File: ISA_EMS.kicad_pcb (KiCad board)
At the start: 2 copper layers, 176.5 x 102.9 mm, 57 parts, among them J1 ISA BUS, J2 EMS Address, J3 ROM Config, U1 74HCT688, U10 74HCT32, U11 74HCT04, U12 74ACT245, U13 AS6C4008-55PCN, U14 AS6C4008-55PCN, U15 AS6C4008-55PCN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

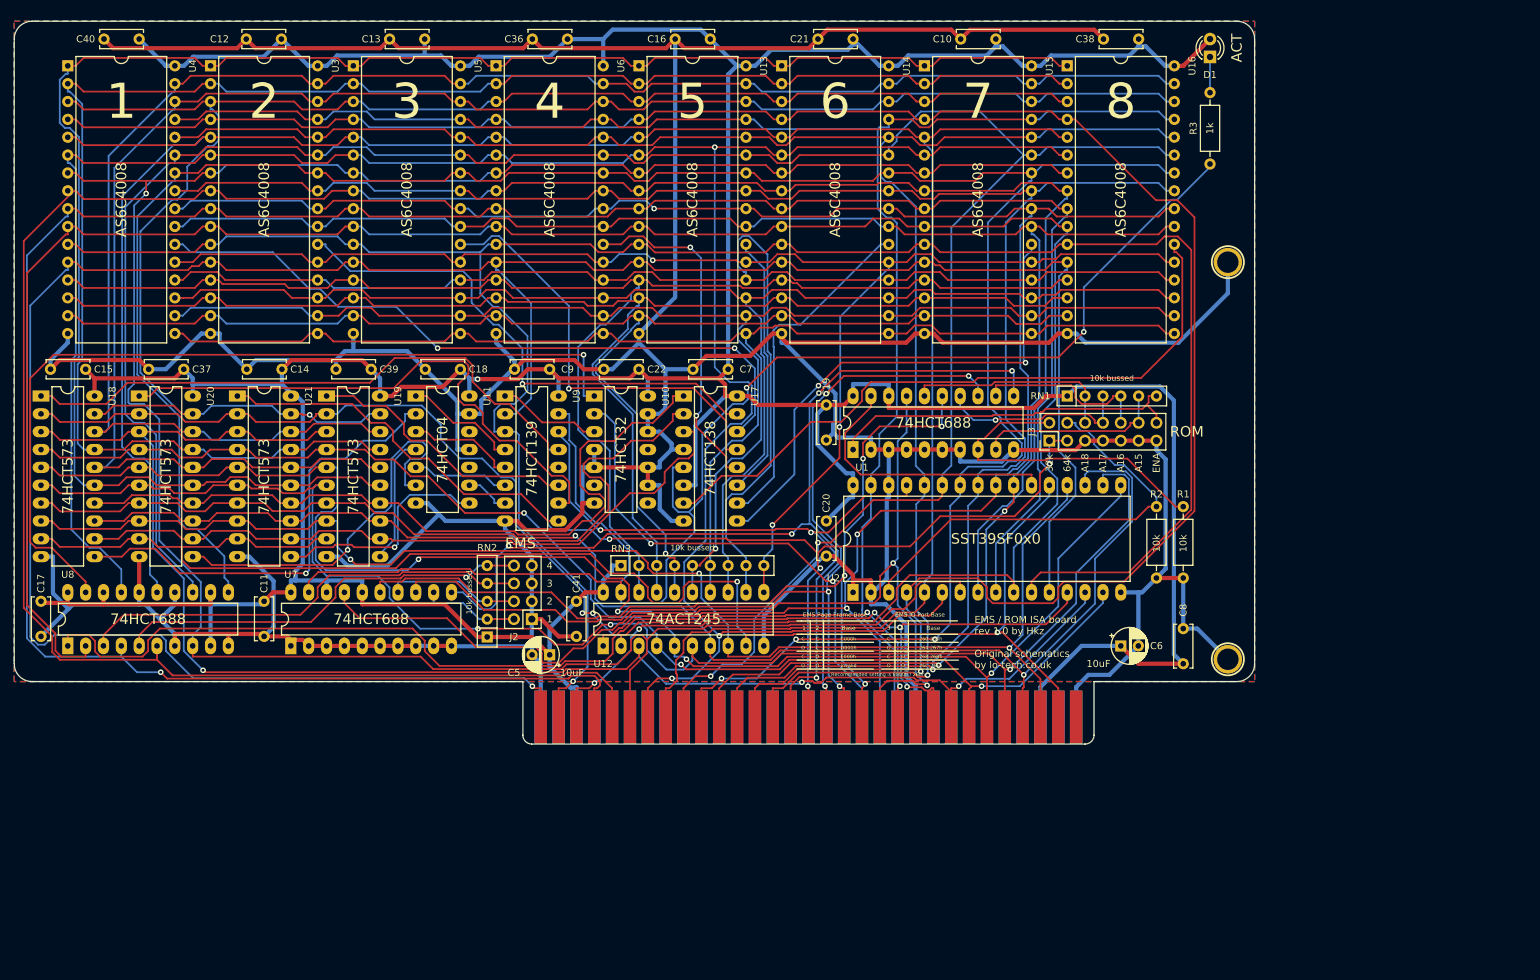
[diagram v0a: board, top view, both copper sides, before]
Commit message: Begin removing useless components
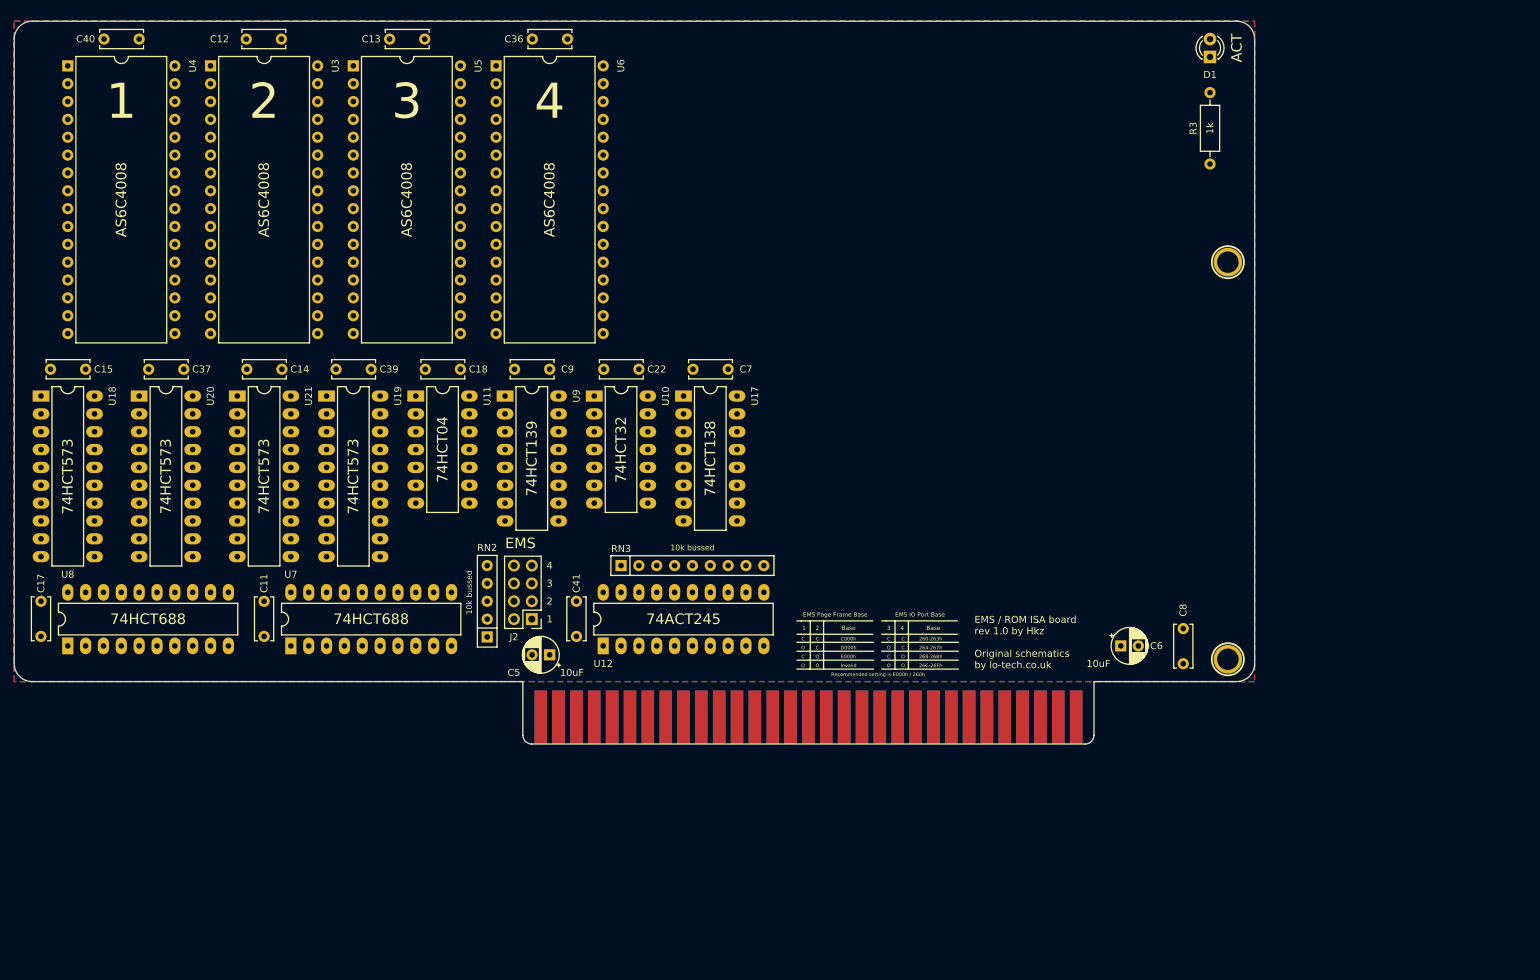
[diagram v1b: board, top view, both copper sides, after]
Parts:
- removed C10, C16, C19, C20, C21, C38: 100nF, Capacitor_THT:C_Disc_D6.0mm_W2.5mm_P5.00mm
- removed J3: ROM Config, Connector_PinHeader_2.54mm:PinHeader_2x07_P2.54mm_Vertical
- removed R1, R2: 10k, Resistor_THT:R_Axial_DIN0207_L6.3mm_D2.5mm_P10.16mm_Horizontal
- removed RN1: 10k, Resistor_THT:R_Array_SIP6
- removed U1: 74HCT688, Package_DIP:DIP-20_W7.62mm_LongPads
- removed U13, U14, U15, U16: AS6C4008-55PCN, Package_DIP:DIP-32_W15.24mm
- removed U2: SST39SF040, Package_DIP:DIP-32_W15.24mm_LongPads
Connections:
- U17 pad 10: /~RAM-CS5 -> (no net)
- U17 pad 11: /~RAM-CS4 -> (no net)
- U17 pad 7: /~RAM-CS7 -> (no net)
- U17 pad 9: /~RAM-CS6 -> (no net)
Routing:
- net GND: track 884.8 -> 0.00 mm
- net VCC: track 681.1 -> 0.00 mm, vias 1 -> 0
- net /A4: track 370.6 -> 0.00 mm
- net /A3: track 363.3 -> 0.00 mm, vias 1 -> 0
- net /A0: track 362.7 -> 0.00 mm, vias 1 -> 0
- net /A5: track 354.4 -> 0.00 mm, vias 1 -> 0
- net /A2: track 353.8 -> 0.00 mm, vias 2 -> 0
- net /A6: track 349.8 -> 0.00 mm, vias 3 -> 0
- net /A7: track 340.5 -> 0.00 mm
- net /A9: track 337.3 -> 0.00 mm, vias 3 -> 0
- net /A8: track 334.0 -> 0.00 mm, vias 2 -> 0
- net /A1: track 315.3 -> 0.00 mm, vias 1 -> 0
- net /A12: track 306.1 -> 0.00 mm, vias 1 -> 0
- net /~MEMR: track 282.7 -> 0.00 mm, vias 3 -> 0
- net /A11: track 261.1 -> 0.00 mm, vias 1 -> 0
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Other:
- board text removed: "10k"
- board text removed: "32k"
- board text removed: "5"
- board text removed: "6"
- board text removed: "64k"
- board text removed: "7"
- board text removed: "8"
- board text removed: "A15"
- board text removed: "A16"
- board text removed: "A17"
- board text removed: "A18"
- board text removed: "ENA"
- board text removed: "ROM"
- board text removed: "SST39SF0x0"

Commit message: Begin moving components
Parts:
- moved U5 81.3 mm to (268.0, 106.7)
- moved U6 81.3 mm to (288.3, 106.7)
- moved C12 81.3 mm to (252.7, 102.9)
- moved C13 81.3 mm to (278.1, 102.9)
- moved C36 81.3 mm to (298.4, 102.9)
- moved C40 81.3 mm to (237.5, 102.9)
- moved U3 81.3 mm to (247.7, 106.7)
- moved U4 81.3 mm to (227.3, 106.7)
- moved C39 69.6 mm to (258.8, 149.6)
- moved U10 69.6 mm to (290.6, 153.4)
- moved C14 69.6 mm to (246.1, 149.6)
- moved C15 69.6 mm to (218.2, 149.6)
- moved C18 69.6 mm to (271.5, 149.6)
- moved C37 69.6 mm to (232.2, 149.6)
- moved C9 69.6 mm to (284.2, 149.6)
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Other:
- board text added: "EMS 2MB ISA board rev 1.0 by Hkz Original schematics by lo-tech.co.uk"
- board text removed: "EMS / ROM ISA board rev 1.0 by Hkz Original schematics by lo-tech.co.uk"

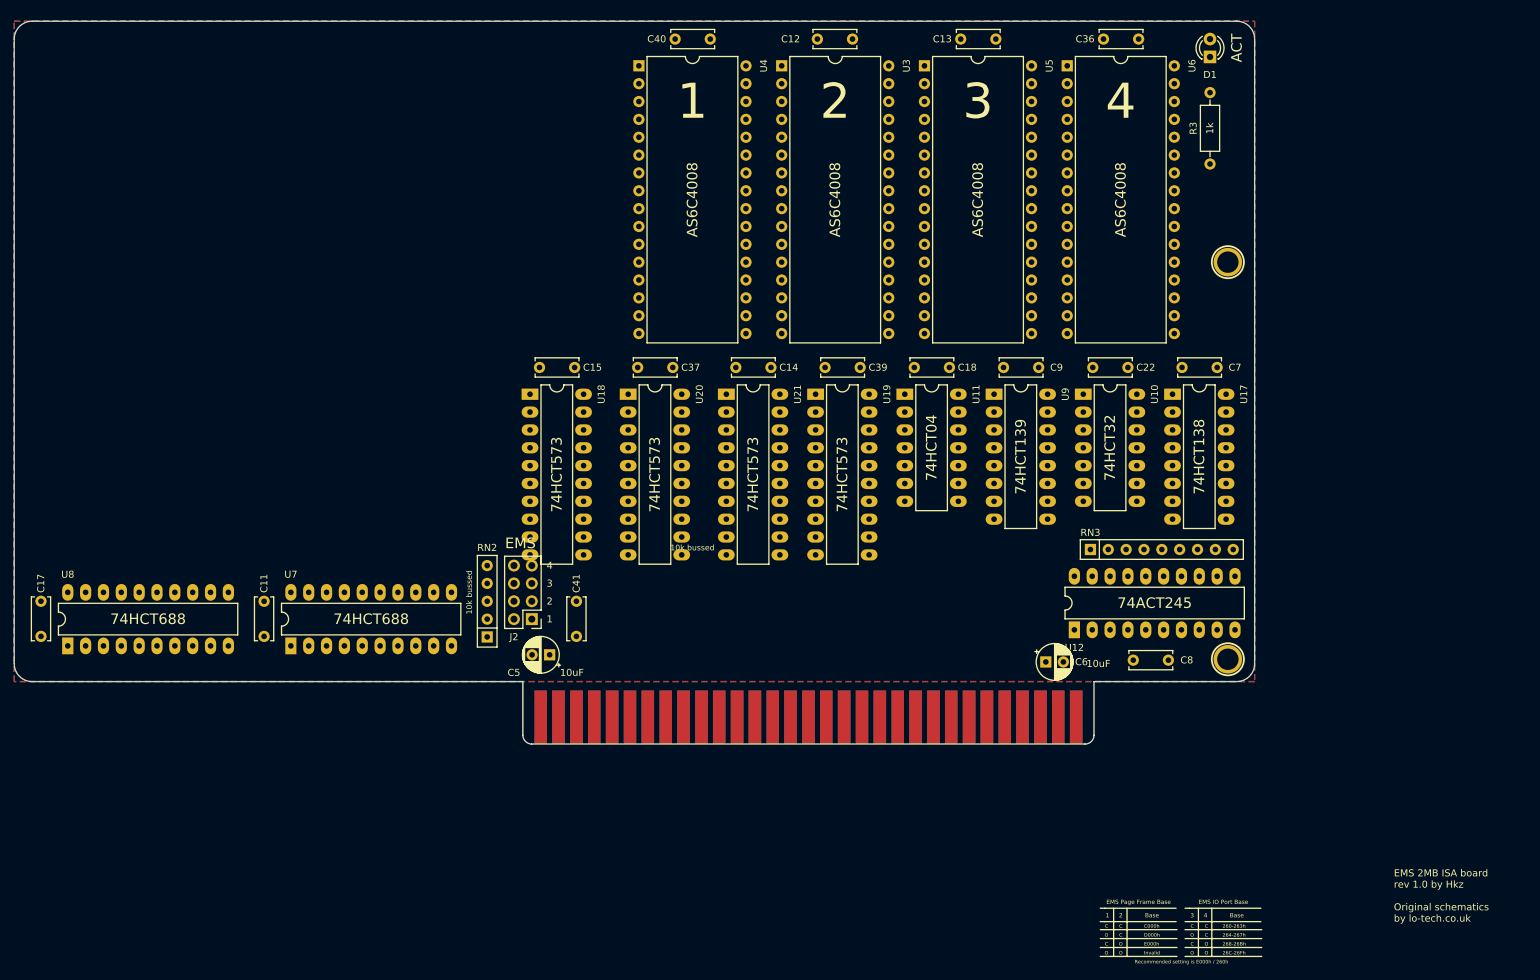
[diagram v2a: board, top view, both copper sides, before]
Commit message: moved components on card
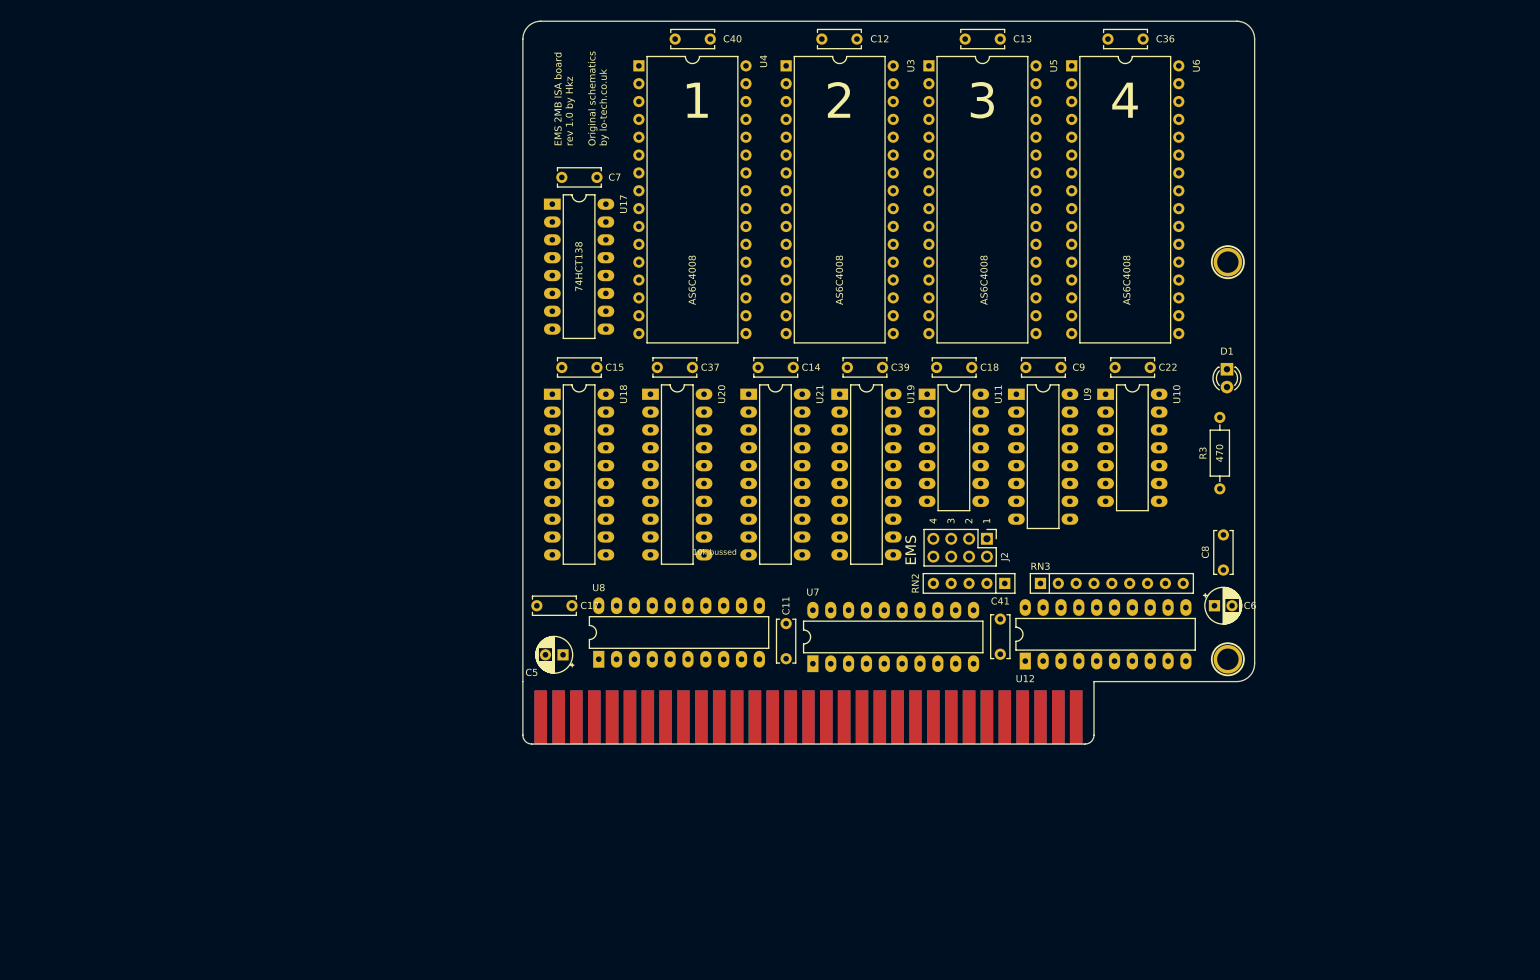
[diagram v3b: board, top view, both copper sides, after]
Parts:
- R3: value 1k -> 470
- U3, U4, U5, U6: value AS6C4008-55PCN -> AS6C4008
- moved U17 92.3 mm to (215.0, 126.4)
- moved C7 92.3 mm to (221.4, 122.6)
- moved U8 75.6 mm to (221.6, 191.1)
- moved C17 75.6 mm to (217.8, 183.5), turned to 180 degrees
- moved C11 74.4 mm to (248.3, 186.1)
- moved U7 74.3 mm to (252.1, 191.8)
- moved RN2 74.1 mm to (279.4, 180.3), turned to 180 degrees
- moved J2 65.8 mm to (276.9, 174.0), turned to 270 degrees
- moved C41 60.4 mm to (278.8, 185.4)
- moved R3 46.2 mm to (310.0, 166.9)
- moved D1 44.5 mm to (311.0, 149.9), turned to 270 degrees
- moved C6 25.3 mm to (309.2, 183.5)
- moved C8 18.1 mm to (310.5, 178.4), turned to 90 degrees
- moved RN3 8.59 mm to (284.5, 180.3)
- moved U12 8.28 mm to (282.3, 191.4)
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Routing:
- removed copper zone on B.Cu, net GND
- removed copper zone on F.Cu, net GND
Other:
- board size 176.5 x 102.9 mm -> 104.1 x 102.9 mm
- board text removed: "10uF"
- board text removed: "1k"
- board text removed: "74ACT245"
- board text removed: "74HCT04"
- board text removed: "74HCT138"
- board text removed: "74HCT139"
- board text removed: "74HCT32"
- board text removed: "74HCT573"
- board text removed: "74HCT688"
- board text removed: "ACT"
- board text removed: "AS6C4008"

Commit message: Add silkscreen
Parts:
- U18, U19, U20, U21: value 74LS573 -> 74HCT573
- U3, U4, U5, U6: value AS6C4008 -> AS6C4008-55PCN
- moved RN3 0.90 mm to (285.1, 179.7)
- moved C11 0.64 mm to (248.3, 185.4)
- moved U7 0.64 mm to (252.1, 191.1)
- moved C6 0.63 mm to (309.9, 183.5)
- moved U12 0.25 mm to (282.3, 191.1)
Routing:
- net GND: track 0.00 -> 567.4 mm
- net VCC: track 0.00 -> 478.1 mm, vias 0 -> 1
- net /~RAM-SELECT: track 0.00 -> 271.8 mm, vias 0 -> 1
- net /A0: track 0.00 -> 179.6 mm
- net /RAM-A14: track 0.00 -> 174.0 mm, vias 0 -> 1
- net /A1: track 0.00 -> 172.4 mm, vias 0 -> 1
- net /A5: track 0.00 -> 172.3 mm
- net /RAM-A18: track 0.00 -> 170.6 mm
- net /RAM-A16: track 0.00 -> 163.7 mm
- net /A4: track 0.00 -> 163.6 mm, vias 0 -> 1
- net /~MEMW: track 0.00 -> 161.9 mm
- net /RAM-A15: track 0.00 -> 161.7 mm
- net /RAM-A17: track 0.00 -> 160.6 mm
- net /~MEMR: track 0.00 -> 159.6 mm, vias 0 -> 1
- net /A7: track 0.00 -> 157.1 mm, vias 0 -> 1
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- added copper zone on B.Cu, net GND
- added copper zone on F.Cu, net GND
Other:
- board text removed: "10k bussed"

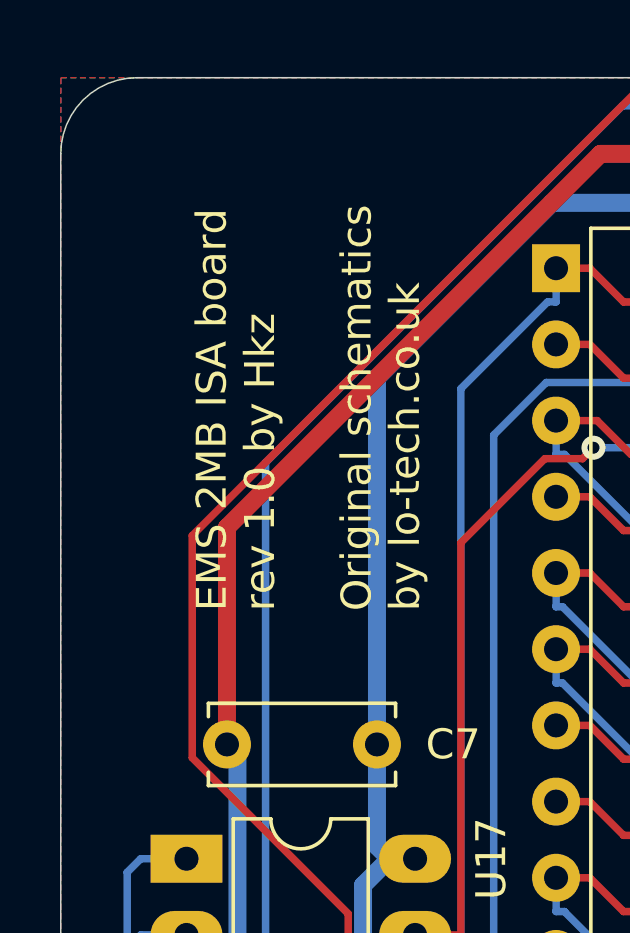
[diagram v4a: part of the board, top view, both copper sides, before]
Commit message: add via to board and refill
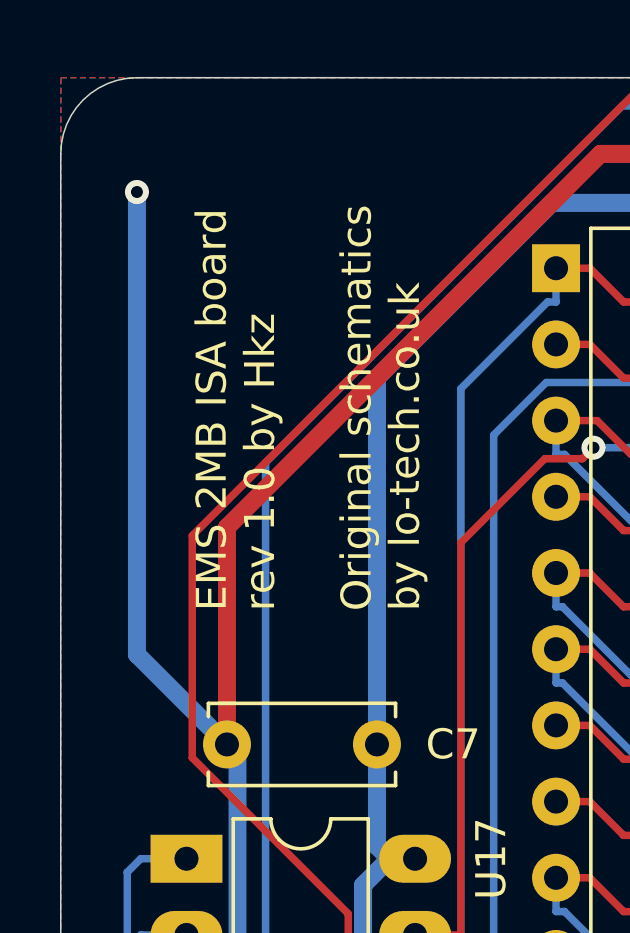
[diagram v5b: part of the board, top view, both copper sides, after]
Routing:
- net GND: track 567.4 -> 587.1 mm, vias 0 -> 1
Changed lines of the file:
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@@
     (thickness 1.6)
     (drawings 83)
-    (tracks 2016)
+    (tracks 2019)
     (zones 0)
     (modules 41)
@@
   (page A3)
   (layers
-    (0 F.Cu signal hide)
-    (31 B.Cu signal hide)
+    (0 F.Cu signal)
+    (31 B.Cu signal)
     (32 B.Adhes user)
     (33 F.Adhes user)
@@
     (arrow2b (pts (xy 314.96 199.39) (xy 313.833496 199.976421)))
   )
+  (via (at 213.36 104.14) (size 0.8) (drill 0.4) (layers F.Cu B.Cu) (net 1))
   (segment (start 232.7774 177.9474) (end 232.7774 180.8123) (width 0.6) (layer F.Cu) (net 1))
   (segment (start 232.7774 180.8123) (end 231.775 181.8147) (width 0.6) (layer F.Cu) (net 1))
@@
   (segment (start 213.36 191.175) (end 214.035 190.5) (width 0.6) (layer B.Cu) (net 1))
   (segment (start 215.011 133.985) (end 216.7113 133.985) (width 0.6) (layer B.Cu) (net 1))
+  (segment (start 213.36 119.554) (end 216.361 122.555) (width 0.6) (layer B.Cu) (net 1))
+  (segment (start 213.36 104.14) (end 213.36 119.554) (width 0.6) (layer B.Cu) (net 1))
   (segment (start 284.48 199.39) (end 284.48 195.0797) (width 0.6) (layer B.Cu) (net 2))
   (segment (start 278.765 185.42) (end 278.765 187.5557) (width 0.6) (layer B.Cu) (net 2))
@@
     (connect_pads (clearance 0.508))
     (min_thickness 0.254)
-    (fill (arc_segments 32) (thermal_gap 0.508) (thermal_bridge_width 0.508))
+    (fill yes (arc_segments 32) (thermal_gap 0.508) (thermal_bridge_width 0.508))
     (polygon
       (pts
@@
     (connect_pads (clearance 0.508))
     (min_thickness 0.254)
-    (fill (arc_segments 32) (thermal_gap 0.508) (thermal_bridge_width 0.508))
+    (fill yes (arc_segments 32) (thermal_gap 0.508) (thermal_bridge_width 0.508))
     (polygon
       (pts
